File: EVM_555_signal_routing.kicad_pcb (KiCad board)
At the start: 2 copper layers, 80 x 50.2 mm, 60 parts, among them J1 GND, J1A1 GND, J2 trig, J2A1 trig, J3 op, J3A1 op, J4 rst, J4A1 rst, J5 ctrl_v, J5A1 ctrl_v, J6 thresh, J6A1 thresh, J7 dis_q, J7A1 dis_q, J8 VCC, J8A1 VCC, Q1 MMBT3904, Q10 MMBT3906, Q11 MMBT3906, Q12 MMBT3906, Q13 MMBT3906, Q14 MMBT3904, Q15 MMBT3904, Q16 MMBT3904, Q17 MMBT3904, Q18 MMBT3904, Q19A1 MMBT3906, Q19B1 MMBT3906, Q2 MMBT3904, Q20 MMBT3904, Q21 MMBT3904, Q22 MMBT3904, Q23 MMBT3906, Q24 MMBT3904, Q25 MMBT3906, Q3 MMBT3904, Q4 MMBT3904, Q5 MMBT3906, Q6 MMBT3906, Q7 MMBT3906, Q8 MMBT3906, Q9 MMBT3906

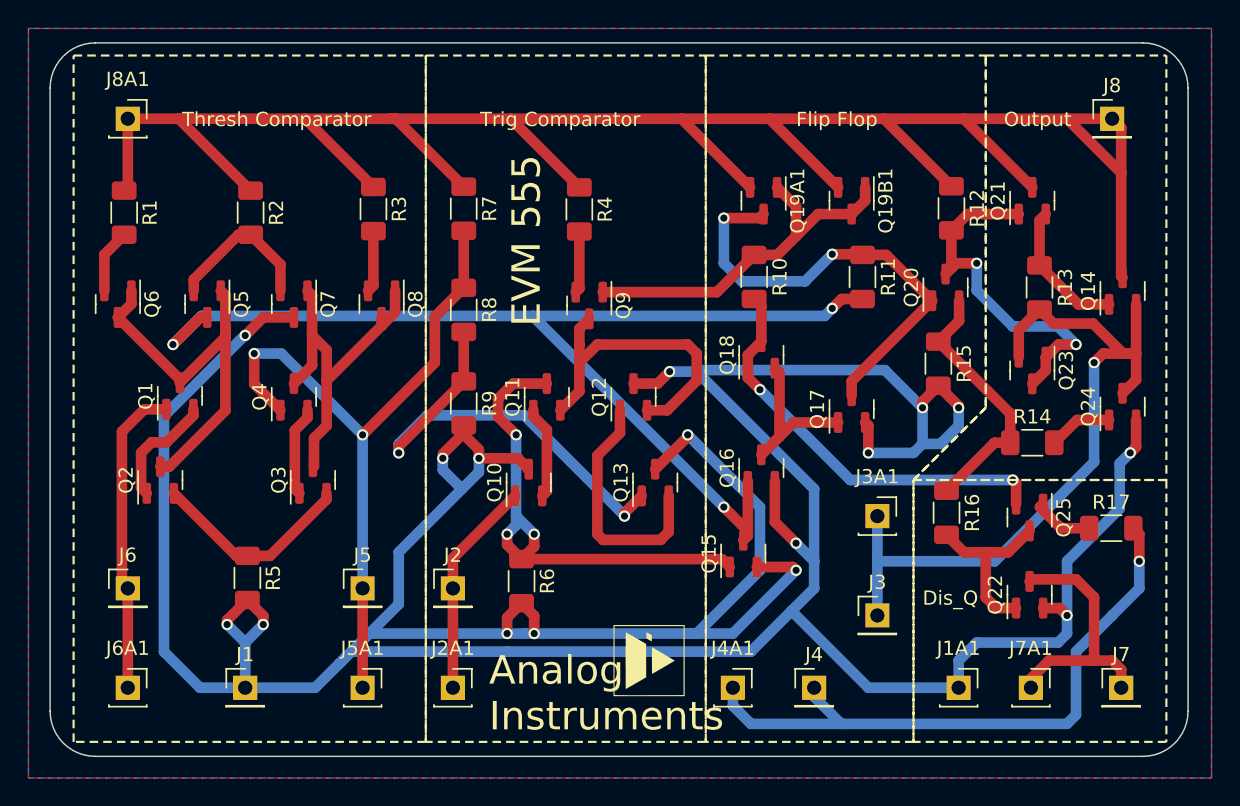
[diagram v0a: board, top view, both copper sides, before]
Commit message: fixed silkscreen
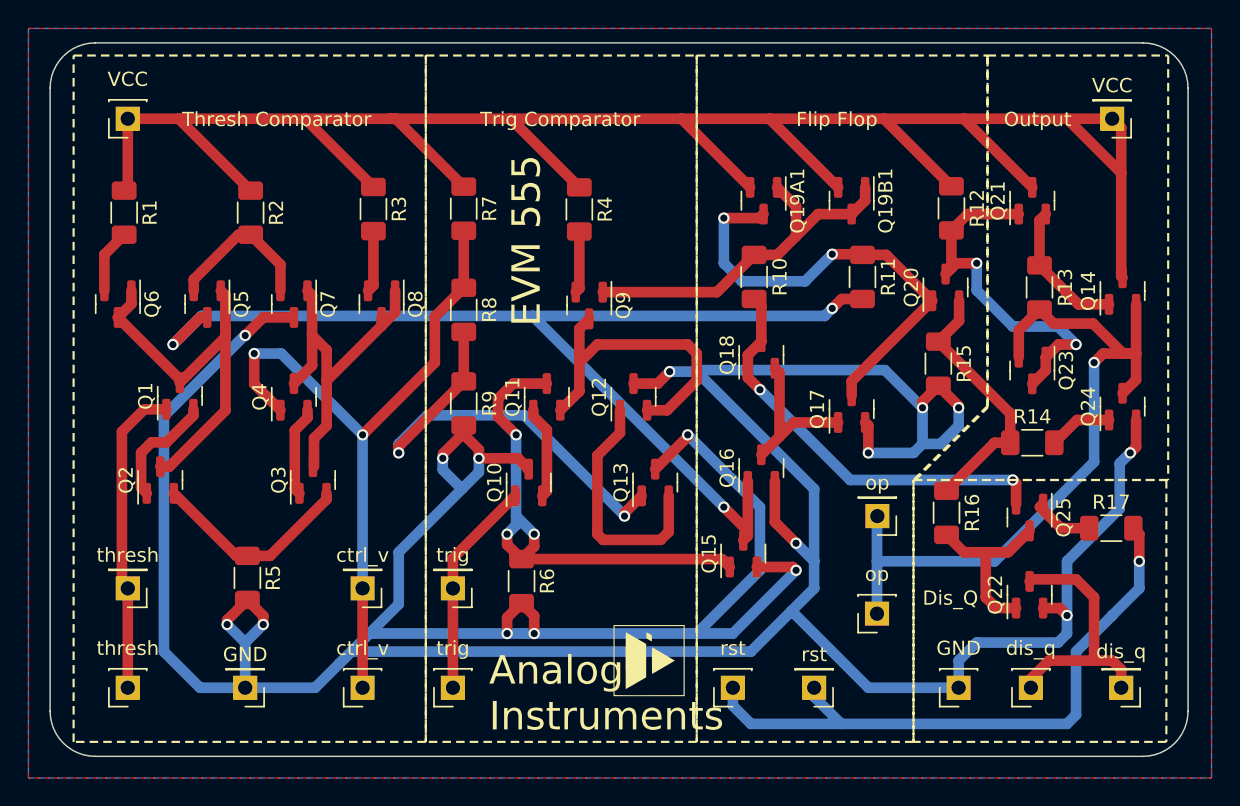
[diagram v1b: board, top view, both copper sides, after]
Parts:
- moved J3 6.98 mm to (120.0, 66.0), turned to 180 degrees
- moved J3A1 6.86 mm to (120.0, 72.9), turned to 180 degrees
- turned J1 to 180 degrees
- turned J1A1 to 180 degrees
- turned J2 to 180 degrees
- turned J2A1 to 180 degrees
- turned J4 to 180 degrees
- turned J4A1 to 180 degrees
- turned J5 to 180 degrees
- turned J5A1 to 180 degrees
- turned J6 to 180 degrees
- turned J6A1 to 180 degrees
- turned J7 to 180 degrees
- turned J7A1 to 180 degrees
- turned J8 to 180 degrees
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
